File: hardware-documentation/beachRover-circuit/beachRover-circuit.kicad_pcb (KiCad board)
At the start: 2 copper layers, 99.1 x 54.6 mm, 3 parts

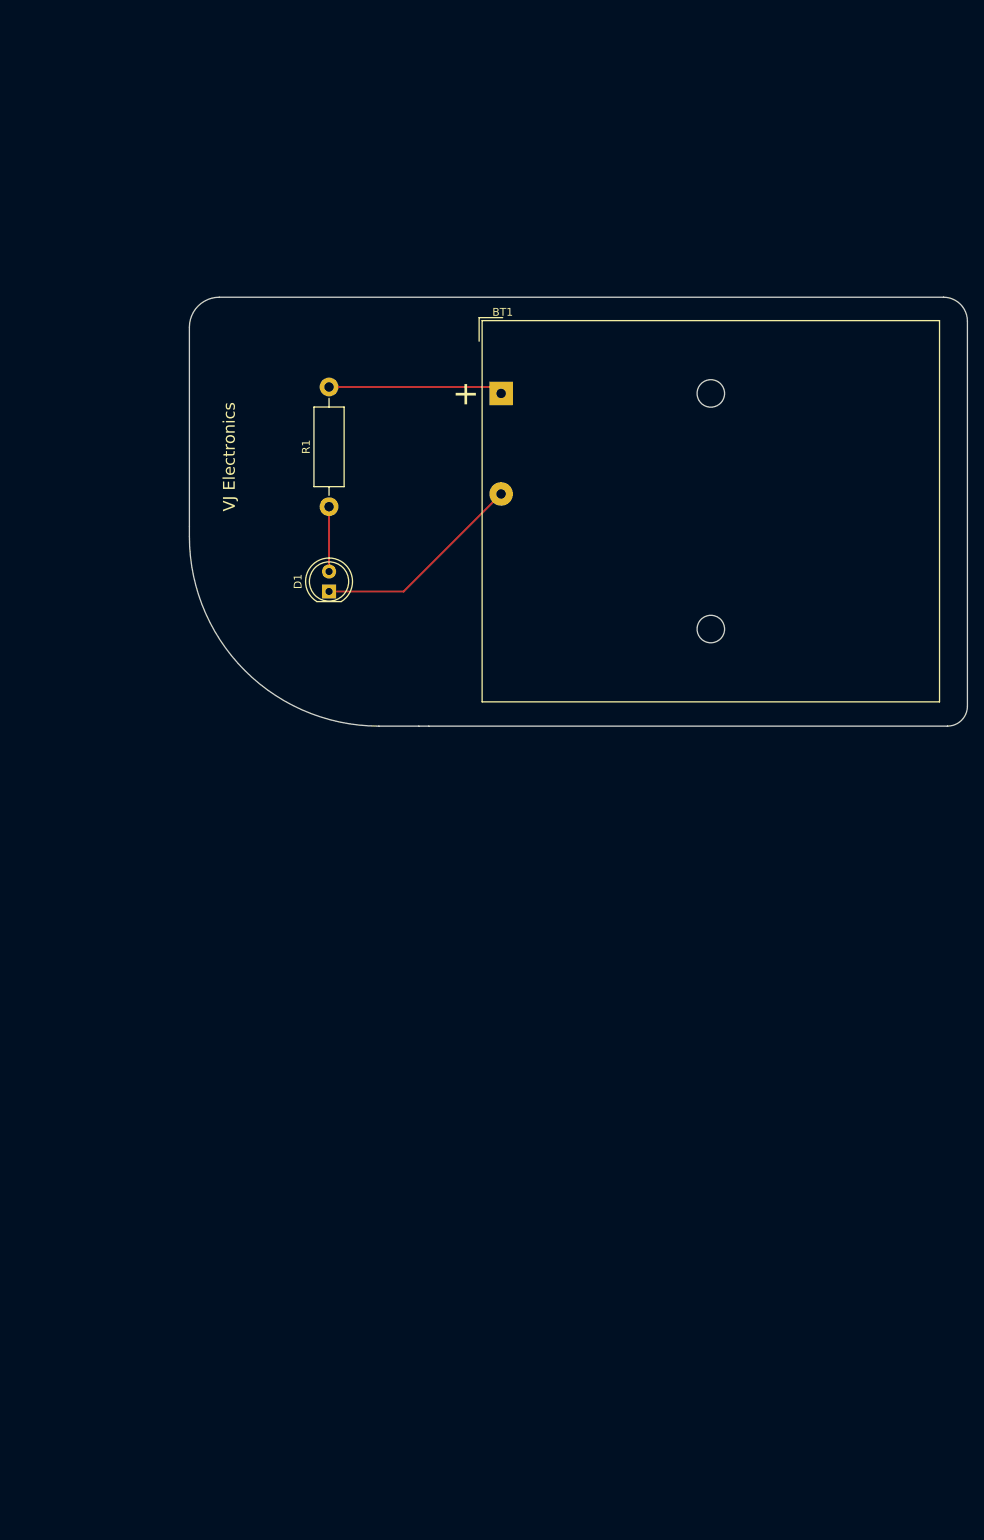
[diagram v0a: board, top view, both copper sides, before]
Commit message: Added few components in schematic and assigned footprints
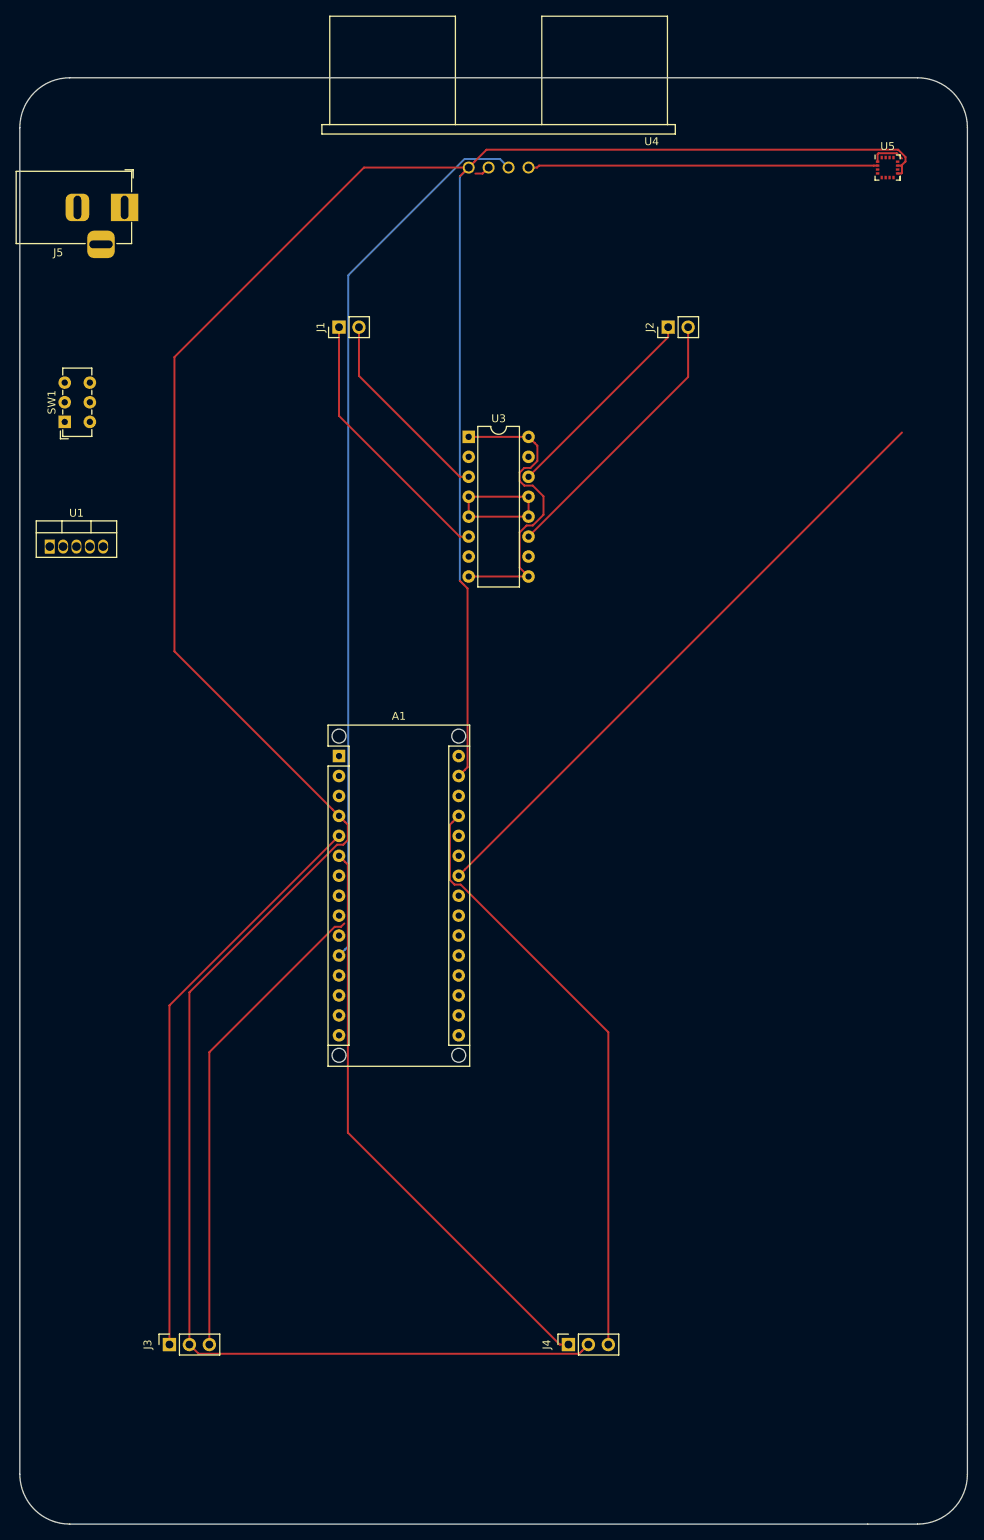
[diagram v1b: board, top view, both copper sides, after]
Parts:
- removed BT1: 5v, Battery:BatteryHolder_TruPower_BH-331P_3xAA
- removed D1: LED, LED_THT:LED_D5.0mm
- removed R1: 330, Resistor_THT:R_Axial_DIN0411_L9.9mm_D3.6mm_P15.24mm_Horizontal
- added A1: Arduino_Nano_v3.x, Module:Arduino_Nano_WithMountingHoles, F.Cu at (97.8, 130.8)
- added J1: Conn_01x02_Male, Connector_PinHeader_2.54mm:PinHeader_1x02_P2.54mm_Vertical, F.Cu at (97.8, 76.2)
- added J2: Conn_01x02_Male, Connector_PinHeader_2.54mm:PinHeader_1x02_P2.54mm_Vertical, F.Cu at (139.7, 76.2)
- added J3: Conn_01x03, Connector_PinSocket_2.54mm:PinSocket_1x03_P2.54mm_Vertical, F.Cu at (76.2, 205.7)
- added J4: Conn_01x03, Connector_PinSocket_2.54mm:PinSocket_1x03_P2.54mm_Vertical, F.Cu at (127.0, 205.7)
- added J5: Barrel_Jack_Switch, Connector_BarrelJack:BarrelJack_Horizontal, F.Cu at (70.5, 61.0)
- added SW1: SW_DIP_x03, Button_Switch_THT:SW_E-Switch_EG1271_DPDT, F.Cu at (62.9, 88.3)
- added U1: LM2575-5.0BT, Package_TO_SOT_THT:TO-220-5_Vertical, F.Cu at (61.0, 104.1)
- added U3: L293D, Package_DIP:DIP-16_W7.62mm, F.Cu at (114.3, 90.2)
- added U4: HC-SR04, HC-SR04:XCVR_HC-SR04, F.Cu at (118.1, 55.9)
- added U5: MMC5883MA, Package_LGA:LGA-16_3x3mm_P0.5mm, F.Cu at (167.6, 55.9)
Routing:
- net Net-(A1-Pad29): track 0.00 -> 404.7 mm
- net Net-(A1-Pad27): track 0.00 -> 182.3 mm
- net Net-(A1-Pad11): track 0.00 -> 114.1 mm
- net Net-(A1-Pad24): track 0.00 -> 84.2 mm
- net Net-(A1-Pad6): track 0.00 -> 75.0 mm
- net Net-(A1-Pad5): track 0.00 -> 73.7 mm
- net Net-(J5-Pad2): track 0.00 -> 39.0 mm
- net Net-(J2-Pad2): track 0.00 -> 35.1 mm
- net Net-(J1-Pad1): track 0.00 -> 34.2 mm
- net Net-(BT1-Pad2): track 27.1 -> 0.00 mm
- net Net-(J2-Pad1): track 0.00 -> 26.4 mm
- net Net-(J1-Pad2): track 0.00 -> 25.5 mm
- net Net-(BT1-Pad1): track 22.9 -> 0.00 mm
- net Net-(D1-Pad2): track 8.25 -> 0.00 mm
- net Net-(A1-Pad10): track 0.00 -> 2.01 mm
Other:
- board size 99.1 x 54.6 mm -> 120.7 x 184.2 mm
- board text removed: "VJ Electronics"
